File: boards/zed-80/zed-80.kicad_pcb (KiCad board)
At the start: 2 copper layers, 99.5 x 70 mm, 34 parts, among them J401 TYPE-C-31-M-12, SW201 SW_Push, U201 GD74LS04, U202 Z84C0010PEC, U301 TT74LS32BI, U302 AT28C256-15PU, U303 HM628128BLP-10, U401 CH340C, U402 MC68B50P, Y201 7.3728 MHz

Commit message: Final touchups and produced fabrication files
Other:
- rule pad_to_mask_clearance: 0 -> 0.1

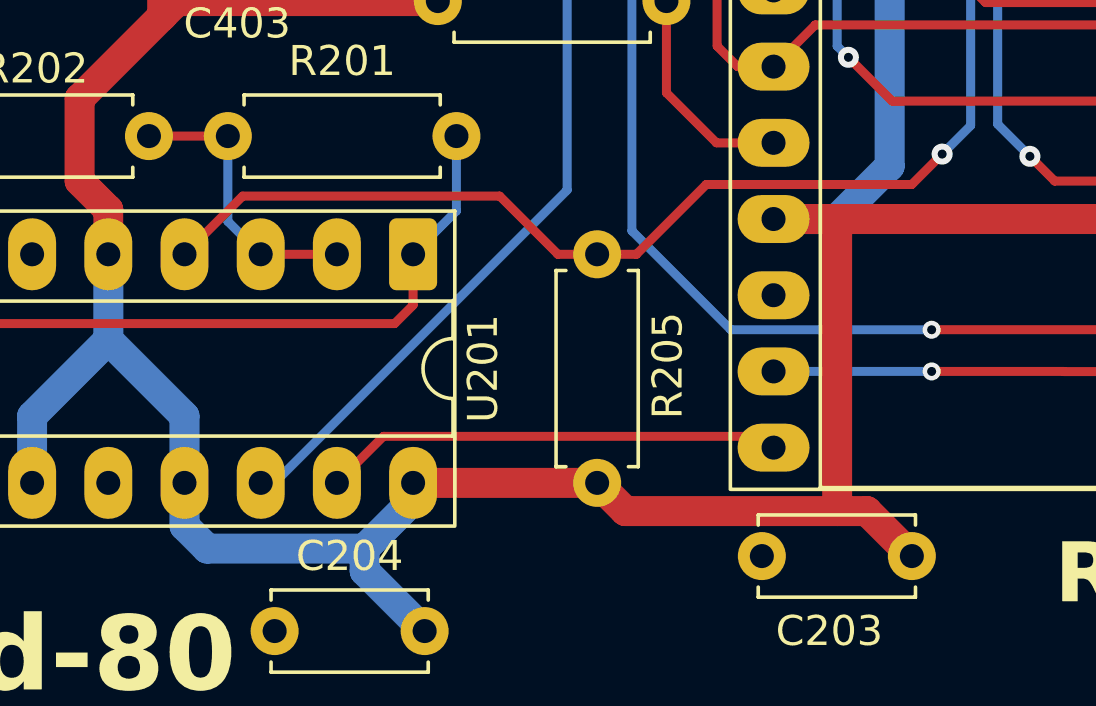
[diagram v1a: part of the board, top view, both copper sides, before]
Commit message: Fixed clock oscillator circuit
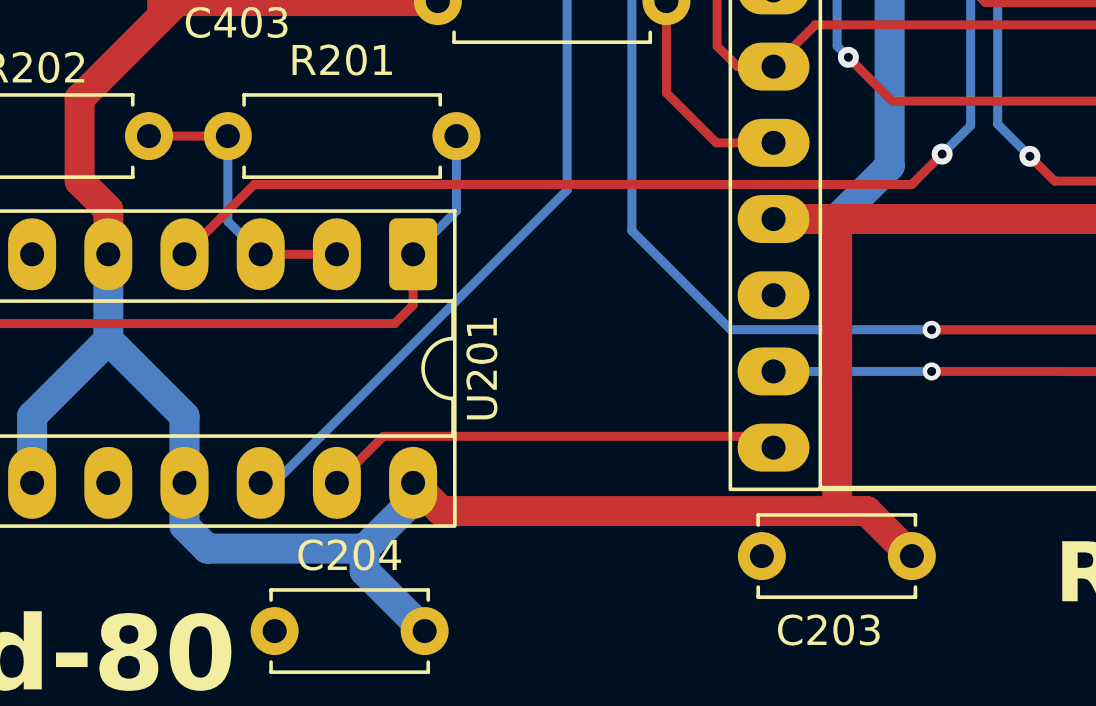
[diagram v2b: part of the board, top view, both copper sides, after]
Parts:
- removed R205: 1 kΩ, Resistor_THT:R_Axial_DIN0207_L6.3mm_D2.5mm_P7.62mm_Horizontal
- R201: value 2 kΩ -> 1 MΩ
- U201: value GD74LS04 -> 74HCT04
- U301: value TT74LS32BI -> 74LS32
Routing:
- net /CPU/CLK: track 81.6 -> 80.0 mm

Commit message: Small tweaks
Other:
- board text added: "Rev. B"
- board text removed: "Rev. A"
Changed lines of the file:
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@@
 	(title_block
 		(title "zed-80")
-		(date "2026-03-17")
+		(date "2026-03-20")
 		(rev "B")
 		(company "Dragos Bajanica")
@@
 		)
 	)
-	(gr_text "Rev. A"
+	(gr_text "Rev. B"
 		(at 162 111.5 0)
 		(layer "F.SilkS" knockout)
@@
 			(justify left bottom)
 		)
-		(render_cache "Rev. A" 0
+		(render_cache "Rev. B" 0
 			(polygon
 				(pts
@@
 			(polygon
 				(pts
-					(xy 172.001011 111.16) (xy 171.572976 111.16) (xy 171.475034 110.698381) (xy 170.988136 110.698381)
-					(xy 170.890195 111.16) (xy 170.462159 111.16) (xy 170.657684 110.362547) (xy 171.058112 110.362547)
-					(xy 171.40225 110.362547) (xy 171.304309 109.870153) (xy 171.263764 109.658883) (xy 171.231646 109.495118)
-					(xy 171.202215 109.65754) (xy 171.161671 109.867344) (xy 171.058112 110.362547) (xy 170.657684 110.362547)
-					(xy 170.962979 109.117397) (xy 171.494574 109.117397)
+					(xy 171.369364 109.125253) (xy 171.487447 109.147633) (xy 171.59105 109.18322) (xy 171.687424 109.234166)
+					(xy 171.765971 109.295198) (xy 171.828942 109.366524) (xy 171.875908 109.448457) (xy 171.904451 109.539966)
+					(xy 171.914305 109.643496) (xy 171.903117 109.755701) (xy 171.871172 109.851063) (xy 171.819173 109.933046)
+					(xy 171.749374 110.00017) (xy 171.66817 110.045927) (xy 171.572976 110.071531) (xy 171.572976 110.077149)
+					(xy 171.681417 110.102858) (xy 171.775819 110.156894) (xy 171.853791 110.234359) (xy 171.912962 110.331772)
+					(xy 171.949336 110.442726) (xy 171.961933 110.569665) (xy 171.951747 110.68446) (xy 171.922219 110.786726)
+					(xy 171.873761 110.878876) (xy 171.80812 110.959996) (xy 171.726694 111.028814) (xy 171.627442 111.085872)
+					(xy 171.519715 111.126094) (xy 171.397905 111.151218) (xy 171.259612 111.16) (xy 170.576831 111.16)
+					(xy 170.576831 110.821479) (xy 170.982519 110.821479) (xy 171.245568 110.821479) (xy 171.334241 110.812588)
+					(xy 171.404722 110.787896) (xy 171.46099 110.748695) (xy 171.503642 110.695525) (xy 171.529995 110.629616)
+					(xy 171.539392 110.547194) (xy 171.530026 110.464737) (xy 171.503692 110.398337) (xy 171.46099 110.344351)
+					(xy 171.404619 110.304372) (xy 171.334137 110.279254) (xy 171.245568 110.270223) (xy 170.982519 110.270223)
+					(xy 170.982519 110.821479) (xy 170.576831 110.821479) (xy 170.576831 109.940006) (xy 170.982519 109.940006)
+					(xy 171.228838 109.940006) (xy 171.308394 109.931978) (xy 171.371506 109.90969) (xy 171.421789 109.874305)
+					(xy 171.460025 109.826466) (xy 171.483467 109.768255) (xy 171.491765 109.696618) (xy 171.483334 109.623251)
+					(xy 171.459791 109.565249) (xy 171.421789 109.519054) (xy 171.371714 109.485218) (xy 171.308605 109.463784)
+					(xy 171.228838 109.456039) (xy 170.982519 109.456039) (xy 170.982519 109.940006) (xy 170.576831 109.940006)
+					(xy 170.576831 109.117397) (xy 171.234455 109.117397)
 				)
 			)
